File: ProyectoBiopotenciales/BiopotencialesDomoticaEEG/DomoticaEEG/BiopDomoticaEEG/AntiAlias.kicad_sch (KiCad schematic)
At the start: 13 parts

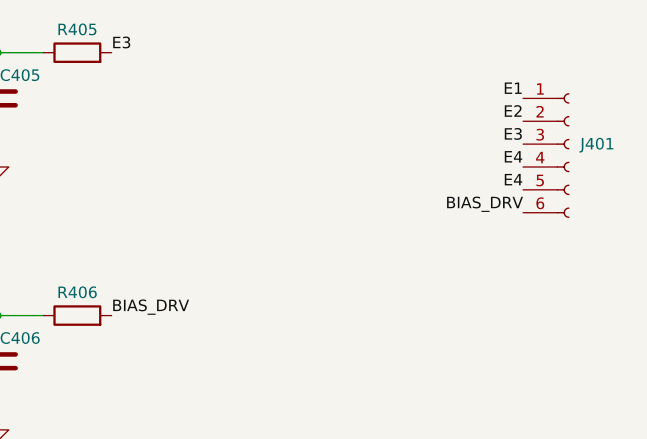
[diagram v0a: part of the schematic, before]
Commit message: feat: more info for block diagram
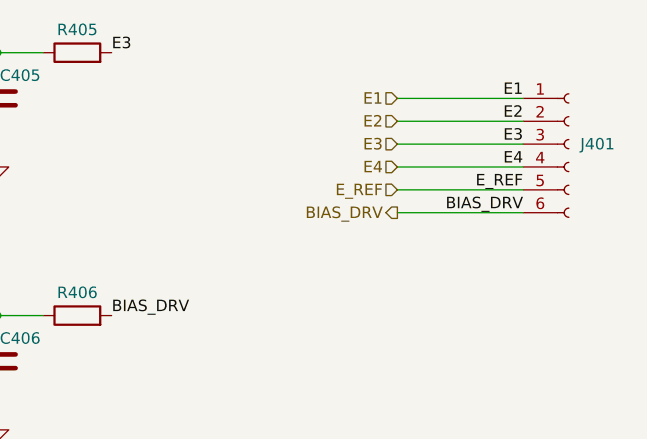
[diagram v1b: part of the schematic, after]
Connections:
- net E4: no longer J401.5 (Pin_5)
- net E_REF: now also J401.5 (Pin_5)
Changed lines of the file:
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@@
   (junction (at 175.26 50.8) (diameter 0) (color 0 0 0 0)
+  )
+  (wire (pts (xy 219.71 58.42) (xy 233.68 58.42))
+    (stroke (width 0) (type default) (color 0 0 0 0))
   )
   (wire (pts (xy 132.08 52.07) (xy 132.08 50.8))
@@
     (stroke (width 0) (type default) (color 0 0 0 0))
   )
+  (wire (pts (xy 219.71 68.58) (xy 233.68 68.58))
+    (stroke (width 0) (type default) (color 0 0 0 0))
+  )
   (wire (pts (xy 171.45 80.01) (xy 175.26 80.01))
     (stroke (width 0) (type default) (color 0 0 0 0))
@@
     (stroke (width 0) (type default) (color 0 0 0 0))
   )
+  (wire (pts (xy 219.71 63.5) (xy 233.68 63.5))
+    (stroke (width 0) (type default) (color 0 0 0 0))
+  )
   (wire (pts (xy 132.08 88.9) (xy 132.08 91.44))
     (stroke (width 0) (type default) (color 0 0 0 0))
@@
     (stroke (width 0) (type default) (color 0 0 0 0))
   )
+  (wire (pts (xy 219.71 55.88) (xy 233.68 55.88))
+    (stroke (width 0) (type default) (color 0 0 0 0))
+  )
   (wire (pts (xy 175.26 81.28) (xy 175.26 80.01))
+    (stroke (width 0) (type default) (color 0 0 0 0))
+  )
+  (wire (pts (xy 219.71 60.96) (xy 233.68 60.96))
     (stroke (width 0) (type default) (color 0 0 0 0))
   )
@@
   )
   (wire (pts (xy 175.26 80.01) (xy 180.34 80.01))
+    (stroke (width 0) (type default) (color 0 0 0 0))
+  )
+  (wire (pts (xy 219.71 66.04) (xy 233.68 66.04))
     (stroke (width 0) (type default) (color 0 0 0 0))
   )
@@
     (effects (font (size 1.27 1.27)) (justify left bottom))
   )
-  (label "E4" (at 233.68 66.04 180)
+  (label "E_REF" (at 233.68 66.04 180)
     (effects (font (size 1.27 1.27)) (justify right bottom))
+  )
+  (hierarchical_label "E1" (shape input) (at 219.71 55.88 180)
+    (effects (font (size 1.27 1.27)) (justify right))
   )
   (hierarchical_label "BIAS_DRV_ADS" (shape input) (at 171.45 80.01 180)
@@
   )
   (hierarchical_label "E_1_ADS" (shape output) (at 77.47 50.8 180)
+    (effects (font (size 1.27 1.27)) (justify right))
+  )
+  (hierarchical_label "E3" (shape input) (at 219.71 60.96 180)
     (effects (font (size 1.27 1.27)) (justify right))
   )
@@
     (effects (font (size 1.27 1.27)) (justify right))
   )
+  (hierarchical_label "E2" (shape input) (at 219.71 58.42 180)
+    (effects (font (size 1.27 1.27)) (justify right))
+  )
+  (hierarchical_label "E_REF" (shape input) (at 219.71 66.04 180)
+    (effects (font (size 1.27 1.27)) (justify right))
+  )
+  (hierarchical_label "BIAS_DRV" (shape output) (at 219.71 68.58 180)
+    (effects (font (size 1.27 1.27)) (justify right))
+  )
   (hierarchical_label "E_2_ADS" (shape output) (at 128.27 50.8 180)
     (effects (font (size 1.27 1.27)) (justify right))
@@
     (effects (font (size 1.27 1.27)) (justify right))
   )
+  (hierarchical_label "E4" (shape input) (at 219.71 63.5 180)
+    (effects (font (size 1.27 1.27)) (justify right))
+  )
